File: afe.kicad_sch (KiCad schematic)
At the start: 142 parts, among them J1 Conn_01x18, Q1 Q_NPN_BCE, Q10 Q_NMOS_GDS, Q11 Q_NMOS_GDS, Q12 Q_NMOS_GDS, Q13 Q_NMOS_GDS, Q14 Q_NMOS_GDS, Q15 Q_NMOS_GDS, Q16 Q_NMOS_GDS, Q17 Q_NMOS_GDS, Q18 Q_NMOS_GDS, Q19 Q_NMOS_GDS, Q2 Q_NMOS_GDS, Q20 Q_NMOS_GDS, Q21 Q_NMOS_GDS, Q3 Q_PMOS_GDS, Q4 Q_NMOS_GDS, Q5 Q_NMOS_GDS, Q6 Q_NMOS_GDS, Q7 Q_NMOS_GDS, Q8 Q_NMOS_GDS, Q9 Q_NMOS_GDS, U1 PB7170

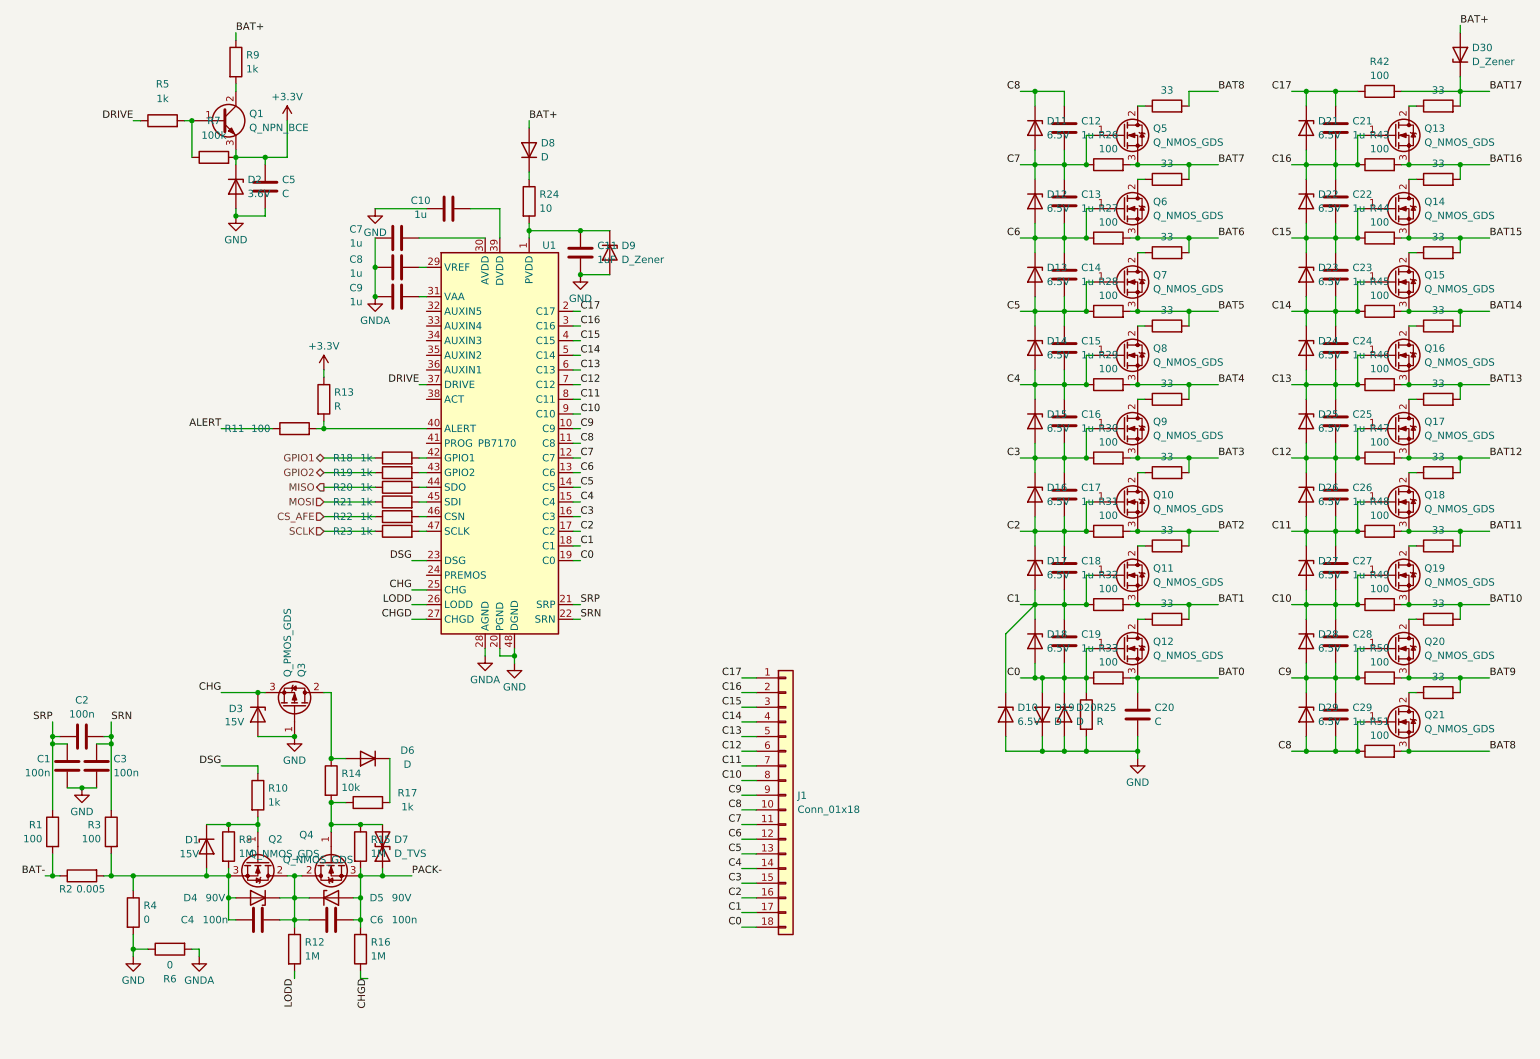
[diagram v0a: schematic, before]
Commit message: fix: 修复commit `38e8c9e`将元器件移动子原理图到造成的位号混乱
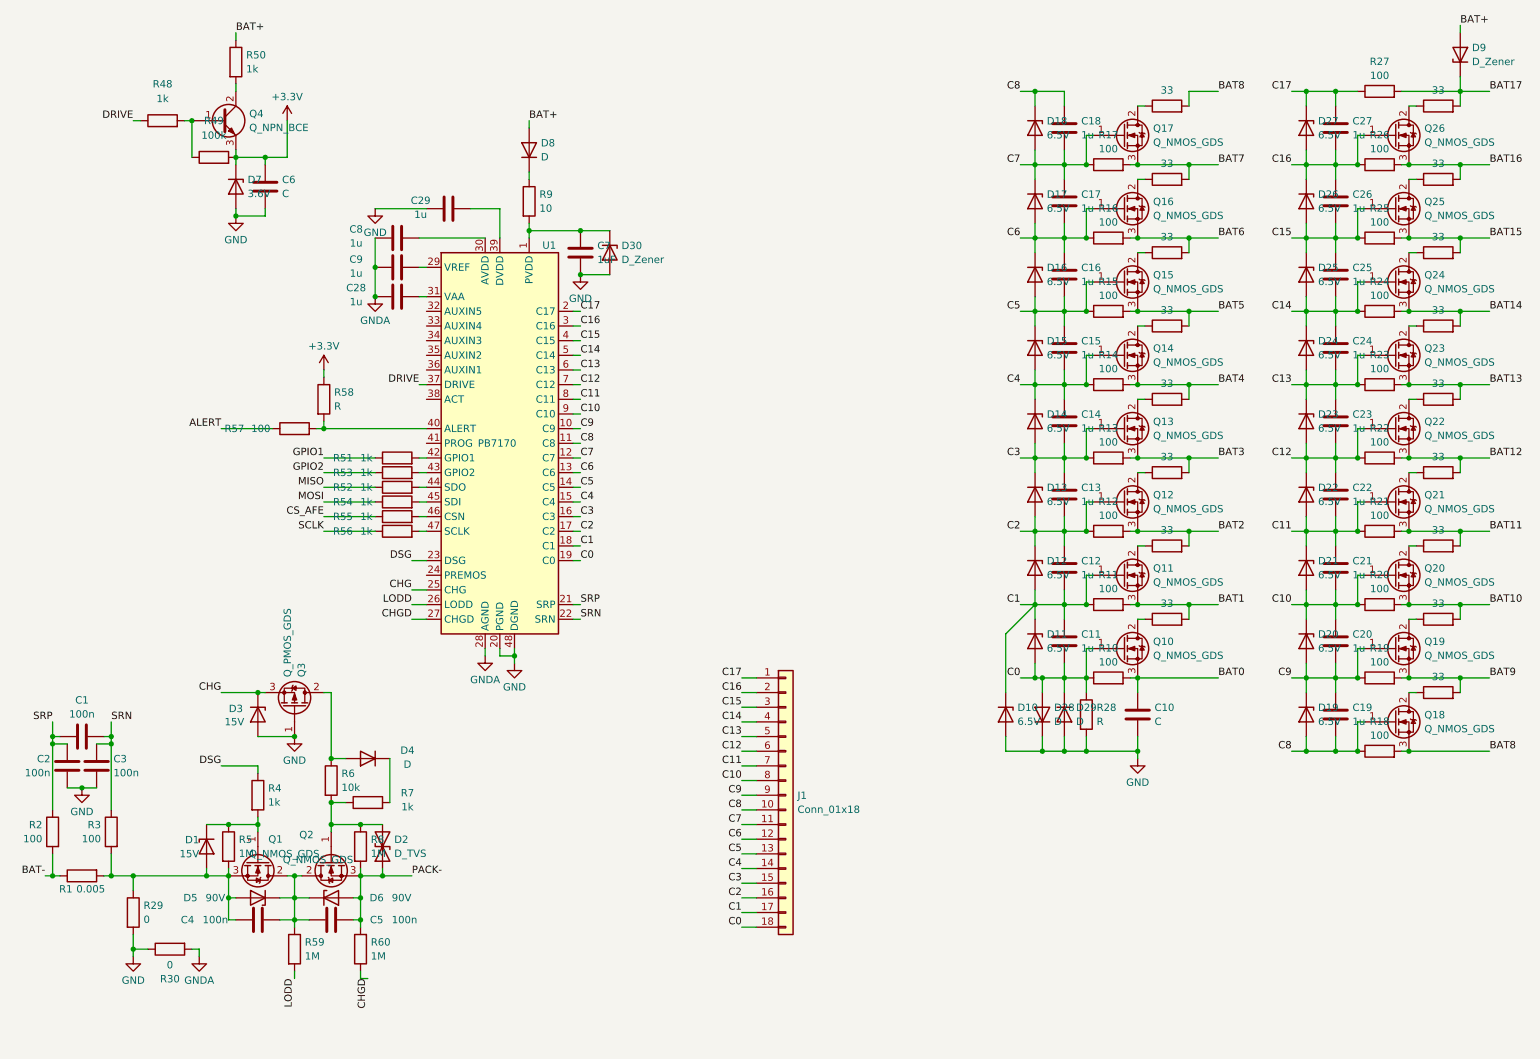
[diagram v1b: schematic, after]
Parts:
- removed D19, D20, D6: D, Diode_SMD:D_SOD-323, symbol Device:D
- removed D2: 3.6V, Diode_SMD:D_SOD-323, symbol Device:D_Zener
- removed D28, D29: 6.5V, Diode_SMD:D_SOD-323, symbol Device:D_Zener
- removed D4: 90V, Diode_SMD:D_SOD-323, symbol Device:D_Zener
- removed D7: D_TVS, Diode_SMD:D_SOD-323, symbol Device:D_TVS
- removed Q1: Q_NPN_BCE, Package_TO_SOT_SMD:SOT-23, symbol Device:Q_NPN_BCE
- removed Q4: Q_NMOS_GDS, Package_TO_SOT_SMD:TO-252-2, symbol Device:Q_NMOS_GDS
- removed Q5, Q6, Q7, Q8, Q9: Q_NMOS_GDS, Package_TO_SOT_SMD:SOT-23, symbol Device:Q_NMOS_GDS
- added D19, D20: 6.5V, Diode_SMD:D_SOD-323, symbol Device:D_Zener
- added D2: D_TVS, Diode_SMD:D_SOD-323, symbol Device:D_TVS
- added D28, D29, D4: D, Diode_SMD:D_SOD-323, symbol Device:D
- added D6: 90V, Diode_SMD:D_SOD-323, symbol Device:D_Zener
- added D7: 3.6V, Diode_SMD:D_SOD-323, symbol Device:D_Zener
- added Q1: Q_NMOS_GDS, Package_TO_SOT_SMD:TO-252-2, symbol Device:Q_NMOS_GDS
- added Q22, Q23, Q24, Q25, Q26: Q_NMOS_GDS, Package_TO_SOT_SMD:SOT-23, symbol Device:Q_NMOS_GDS
- added Q4: Q_NPN_BCE, Package_TO_SOT_SMD:SOT-23, symbol Device:Q_NPN_BCE
- C10: value 1u -> C
- C11: value 1uF -> 1u
- C20: value C -> 1u
- C5: value C -> 100n
- C6: value 100n -> C
- C7: value 1u -> 1uF
- R1: value 100 -> 0.005; footprint Resistor_SMD:R_0603_1608Metric -> Resistor_SMD:R_2512_6332Metric
- R10, R17, R18, R19, R20, R21, R22, R23: value 1k -> 100; footprint Resistor_SMD:R_0402_1005Metric -> Resistor_SMD:R_0603_1608Metric
- R11: footprint Resistor_SMD:R_0402_1005Metric -> Resistor_SMD:R_0603_1608Metric
- R12, R15, R16: value 1M -> 100
- R13, R25: value R -> 100; footprint Resistor_SMD:R_0402_1005Metric -> Resistor_SMD:R_0603_1608Metric
- R14: value 10k -> 100
- R2: value 0.005 -> 100; footprint Resistor_SMD:R_2512_6332Metric -> Resistor_SMD:R_0603_1608Metric
- R24: value 10 -> 100
- R28: value 100 -> R; footprint Resistor_SMD:R_0603_1608Metric -> Resistor_SMD:R_0402_1005Metric
- R29, R30: value 100 -> 0
- R31, R32, R33, R42, R43, R44, R45, R46, R47: value 100 -> 33
- R4: value 0 -> 1k; footprint Resistor_SMD:R_0603_1608Metric -> Resistor_SMD:R_0402_1005Metric
- R48, R51: value 100 -> 1k; footprint Resistor_SMD:R_0603_1608Metric -> Resistor_SMD:R_0402_1005Metric
- R49: value 100 -> 100k
- R5: value 1k -> 1M; footprint Resistor_SMD:R_0402_1005Metric -> Resistor_SMD:R_0603_1608Metric
- R50: value 100 -> 1k
- R52, R53, R54, R55, R56: value 33 -> 1k; footprint Resistor_SMD:R_0603_1608Metric -> Resistor_SMD:R_0402_1005Metric
- R57: value 33 -> 100; footprint Resistor_SMD:R_0603_1608Metric -> Resistor_SMD:R_0402_1005Metric
- R58: value 33 -> R; footprint Resistor_SMD:R_0603_1608Metric -> Resistor_SMD:R_0402_1005Metric
- R59, R60: value 33 -> 1M
- R6: value 0 -> 10k
- R7: value 100k -> 1k; footprint Resistor_SMD:R_0603_1608Metric -> Resistor_SMD:R_0402_1005Metric
- R9: value 1k -> 10
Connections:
- net +3.3V: now also C6.1, R49.2, R58.1, D7.1 (K), Q4.3 (E); no longer C5.1, R13.1, R7.2
- net ALERT: now also R57.1; no longer R11.1
- net BAT+: now also D9.2 (A), R50.1; no longer D30.2 (A), R9.1
- net BAT-: now also R1.1, R2.2; no longer R1.2, R2.1
- net BAT0: now also C10.1, Q10.3 (S), R10.2; no longer C20.1, Q12.3 (S), R33.2
- net BAT1: now also R11.2, R31.2; no longer R32.2, R41.2
- net BAT10: now also Q20.3 (S), R20.2, R40.2; no longer Q19.3 (S), R49.2, R59.2
- net BAT11: now also Q21.3 (S), R21.2, R41.2; no longer Q18.3 (S), R48.2, R58.2
- net BAT12: now also R22.2, R42.2, Q22.3 (S); no longer Q17.3 (S), R47.2, R57.2
- net BAT13: now also R23.2, R43.2, Q23.3 (S); no longer Q16.3 (S), R46.2, R56.2
- net BAT14: now also R24.2, R44.2, Q24.3 (S); no longer Q15.3 (S), R45.2, R55.2
- net BAT15: now also R25.2, R45.2, Q25.3 (S); no longer Q14.3 (S), R44.2, R54.2
- net BAT16: now also R26.2, R46.2, Q26.3 (S); no longer Q13.3 (S), R43.2, R53.2
- net BAT17: now also D9.1 (K), R27.2, R47.2; no longer D30.1 (K), R42.2, R52.2
- net BAT2: now also Q12.3 (S), R12.2, R32.2; no longer Q10.3 (S), R31.2, R40.2
- net BAT3: now also Q13.3 (S), R13.2, R33.2; no longer R30.2, R39.2
- net BAT4: now also Q14.3 (S), R14.2, R34.2; no longer R29.2, R38.2
- net BAT5: now also Q15.3 (S), R15.2, R35.2; no longer R28.2, R37.2
- net BAT6: now also Q16.3 (S), R16.2; no longer R27.2
- net BAT7: now also Q17.3 (S), R17.2, R37.2; no longer R26.2, R35.2
- net BAT8: now also Q18.3 (S), R18.2, R38.2; no longer Q21.3 (S), R34.2, R51.2
- net BAT9: now also Q19.3 (S), R19.2, R39.2; no longer Q20.3 (S), R50.2, R60.2
- net C0: now also C11.2, D11.2 (A), Q10.1 (G), R10.1, R28.1, D28.2 (A), D29.1 (K); no longer C19.2, D18.2 (A), Q12.1 (G), R25.1, R33.1
- net C1: now also C11.1, C12.2, D11.1 (K), D12.2 (A), R11.1; no longer C18.2, C19.1, D17.2 (A), D18.1 (K), R32.1
- net C10: now also C20.1, C21.2, D21.2 (A), Q20.1 (G), R20.1, D20.1 (K); no longer C27.2, C28.1, D27.2 (A), Q19.1 (G), R49.1
- net C11: now also C21.1, C22.2, D21.1 (K), D22.2 (A), Q21.1 (G), R21.1; no longer C26.2, C27.1, D26.2 (A), D27.1 (K), Q18.1 (G), R48.1
- net C12: now also C22.1, C23.2, D22.1 (K), D23.2 (A), R22.1, Q22.1 (G); no longer C25.2, C26.1, D25.2 (A), D26.1 (K), Q17.1 (G), R47.1
- net C13: now also C23.1, D23.1 (K), R23.1, Q23.1 (G); no longer C25.1, D25.1 (K), Q16.1 (G), R46.1
- net C14: now also C25.2, D25.2 (A), R24.1, Q24.1 (G); no longer C23.2, D23.2 (A), Q15.1 (G), R45.1
- net C15: now also C25.1, C26.2, D25.1 (K), D26.2 (A), R25.1, Q25.1 (G); no longer C22.2, C23.1, D22.2 (A), D23.1 (K), Q14.1 (G), R44.1
- net C16: now also C26.1, C27.2, D26.1 (K), D27.2 (A), R26.1, Q26.1 (G); no longer C21.2, C22.1, D21.2 (A), D22.1 (K), Q13.1 (G), R43.1
- net C17: now also C27.1, D27.1 (K), R27.1; no longer C21.1, D21.1 (K), R42.1
- net C2: now also C12.1, C13.2, D12.1 (K), D13.2 (A), Q12.1 (G), R12.1; no longer C17.2, C18.1, D16.2 (A), D17.1 (K), Q10.1 (G), R31.1
- net C3: now also C13.1, C14.2, D13.1 (K), D14.2 (A), Q13.1 (G), R13.1; no longer C16.2, C17.1, D15.2 (A), D16.1 (K), R30.1
- net C4: now also C14.1, D14.1 (K), D15.2 (A), Q14.1 (G), R14.1; no longer C16.1, D14.2 (A), D15.1 (K), R29.1
- net C5: now also C16.2, D15.1 (K), D16.2 (A), Q15.1 (G), R15.1; no longer C14.2, D13.2 (A), D14.1 (K), R28.1
- net C6: now also C16.1, C17.2, D16.1 (K), D17.2 (A), Q16.1 (G), R16.1; no longer C13.2, C14.1, D12.2 (A), D13.1 (K), R27.1
- net C7: now also C17.1, C18.2, D17.1 (K), D18.2 (A), Q17.1 (G), R17.1; no longer C12.2, C13.1, D11.2 (A), D12.1 (K), R26.1
- net C8: now also C18.1, C19.2, D18.1 (K), Q18.1 (G), R18.1, D19.2 (A); no longer C12.1, C29.2, D11.1 (K), Q21.1 (G), R51.1
- net C9: now also C19.1, C20.2, Q19.1 (G), R19.1, D19.1 (K), D20.2 (A); no longer C28.2, C29.1, Q20.1 (G), R50.1
- net CHGD: now also R60.1; no longer R16.1
- net CS_AFE: now also R55.1; no longer R22.1
- net DRIVE: now also R48.1; no longer R5.1
- net DSG: now also R4.1; no longer R10.1
- net GND: now also C10.2, C2.1, C29.1, C6.2, C7.2, D30.2 (A), R28.2, R29.2, R30.1, D28.1 (K), D29.2 (A), D7.2 (A); no longer C1.1, C10.1, C11.2, C20.2, C5.2, D9.2 (A), R25.2, R4.2, R6.1
- net GNDA: now also C28.1, R30.2; no longer C7.1, R6.2
- net GPIO1: now also R51.1; no longer R18.1
- net GPIO2: now also R53.1; no longer R19.1
- net LODD: now also R59.2; no longer R12.2
- net MISO: now also R52.1; no longer R20.1
- net MOSI: now also R54.1; no longer R21.1
- net PACK-: now also C5.2, Q2.3 (S), R60.2, R8.2, D2.1 (A1), D6.2 (A); no longer C6.2, D5.2 (A), R15.2, R16.2
- net SCLK: now also R56.1; no longer R23.1
- net SRN: now also C1.2; no longer C2.2
- net SRP: now also C1.1, C2.2, R2.1; no longer C1.2, C2.1, R1.1
- net at U1.31 (VAA): now also C28.2; no longer C9.2
- net at R37.1: now also Q16.2 (D)
- net at R34.1: now also Q13.2 (D)
- net at Q2.1 (G), R8.1: now also R6.2, R7.1, D2.2 (A2); no longer D1.1 (K), R10.2
- net at C4.2, D5.1 (K), Q2.2 (D): now also C5.1, R59.1, D6.1 (K), Q1.2 (D); no longer C6.1, R12.1
- net at Q20.2 (D): now also R41.1; no longer R59.1
- net at Q12.2 (D): now also R33.1; no longer R41.1
- net at D8.1 (K): now also R9.1; no longer R24.1
- net at U1.44 (SDO): now also R52.2; no longer R20.2
- net at Q18.2 (D): now also R39.1; no longer R57.1
- net at R36.1: now also Q15.2 (D)
- net at R40.1: now also Q19.2 (D); no longer Q11.2 (D)
- net at R5.2: now also C4.1, D1.2 (A), D5.2 (A), R1.2, R29.1, R3.2, Q1.3 (S); no longer R7.1
- net at U1.46 (CSN): now also R55.2; no longer R22.2
- net at Q3.2 (D): now also R6.1, D4.2 (A); no longer R14.1
- net at Q17.2 (D): now also R38.1; no longer R56.1
- net at U1.30 (AVDD): now also C8.2; no longer C7.2
- net at R35.1: now also Q14.2 (D)
- net at U1.42 (GPIO1): now also R51.2; no longer R18.2
- net at U1.43 (GPIO2): now also R53.2; no longer R19.2
- net at R9.2: now also C7.1, D30.1 (K), U1.1 (PVDD)
- net at U1.39 (DVDD): now also C29.2; no longer C10.2
- net at U1.47 (SCLK): now also R56.2; no longer R23.2
- net at Q21.2 (D): now also R42.1; no longer R60.1
- net at Q10.2 (D): now also R31.1; no longer R39.1
- net at U1.29 (VREF): now also C9.2; no longer C8.2
- net at U1.45 (SDI): now also R54.2; no longer R21.2
- new net: Q25.2 (D), R46.1
- new net: D4.1 (K), R7.2
- new net: D1.1 (K), Q1.1 (G), R4.2, R5.1
- new net: Q23.2 (D), R44.1
- new net: Q22.2 (D), R43.1
- new net: Q4.1 (B), R48.2, R49.1
- new net: Q4.2 (C), R50.2
- new net: Q24.2 (D), R45.1
- new net: Q26.2 (D), R47.1
- new net: R57.2, R58.2, U1.40 (ALERT)
- new net: Q11.2 (D), R32.1

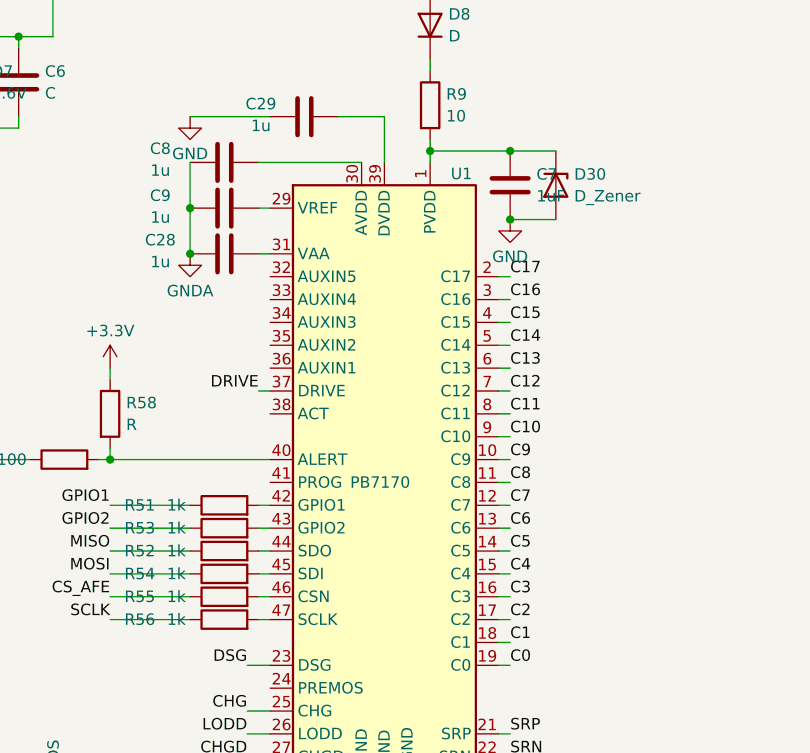
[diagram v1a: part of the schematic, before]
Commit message: 添加PB7170(LQFP-64)符号，原符号重命名为PB7170P48(LQFP-48)并应用于原理图，更新到PCB文件
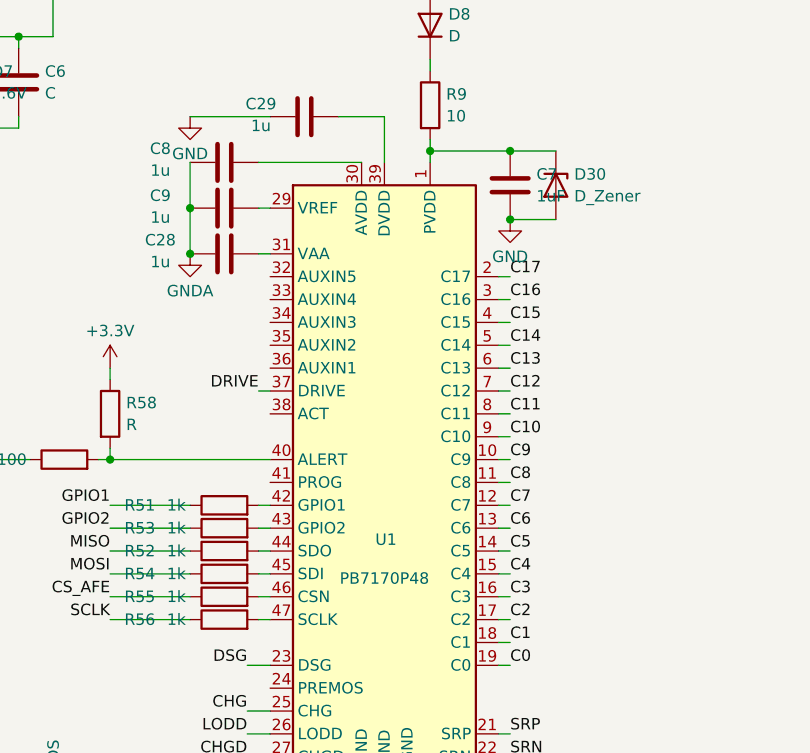
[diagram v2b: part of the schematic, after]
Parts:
- U1: value PB7170 -> PB7170P48; footprint Package_QFP:LQFP-48-1EP_7x7mm_P0.5mm_EP3.6x3.6mm_ThermalVias -> Package_QFP:LQFP-48_7x7mm_P0.5mm; symbol project_symbols:PB7170 -> project_symbols:PB7170P48
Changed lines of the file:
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@@
 	)
 	(symbol
-		(lib_id "project_symbols:PB7170")
+		(lib_id "project_symbols:PB7170P48")
 		(at 101.6 91.44 0)
 		(unit 1)
@@
 		(dnp no)
 		(property "Reference" "U1"
-			(at 108.966 57.15 0)
+			(at 100.584 97.79 0)
 			(effects
 				(font
@@
 			)
 		)
-		(property "Value" "PB7170"
-			(at 97.79 91.44 0)
+		(property "Value" "PB7170P48"
+			(at 101.6 102.108 0)
 			(effects
 				(font
 					(size 1.27 1.27)
 				)
-				(justify left)
 			)
 		)
-		(property "Footprint" "Package_QFP:LQFP-48-1EP_7x7mm_P0.5mm_EP3.6x3.6mm_ThermalVias"
+		(property "Footprint" "Package_QFP:LQFP-48_7x7mm_P0.5mm"
 			(at 124.46 125.73 0)
 			(effects
@@
 			)
 		)
-		(property "Datasheet" "http://www.ti.com/lit/ds/symlink/bq76940.pdf"
+		(property "Datasheet" "http://www.pengshenchip.com/ProductsStd_253.html"
 			(at 119.38 62.23 0)
 			(effects
